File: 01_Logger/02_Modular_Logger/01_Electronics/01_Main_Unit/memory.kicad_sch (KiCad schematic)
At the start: 3 parts, among them J701 Micro_SD_Card_Det

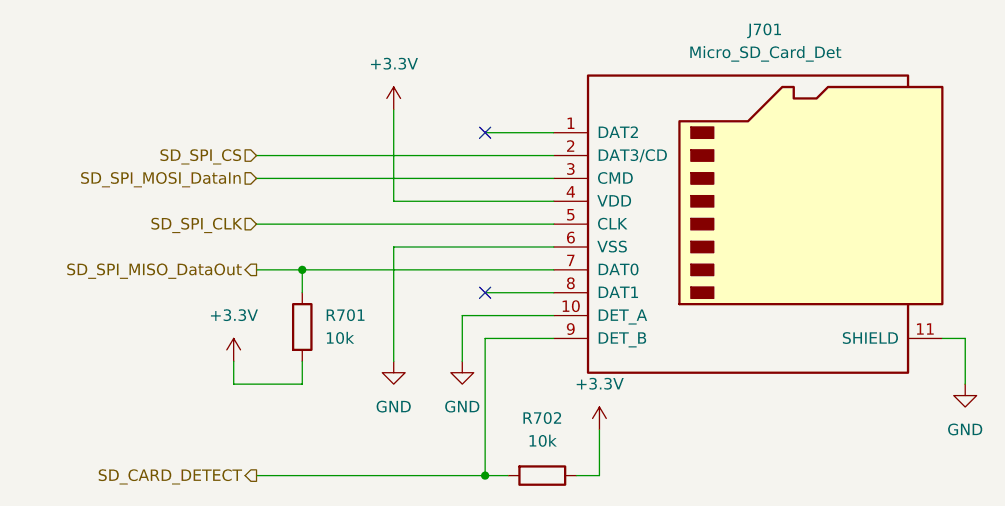
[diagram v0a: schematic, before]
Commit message: update Electronics for Modular_Logger
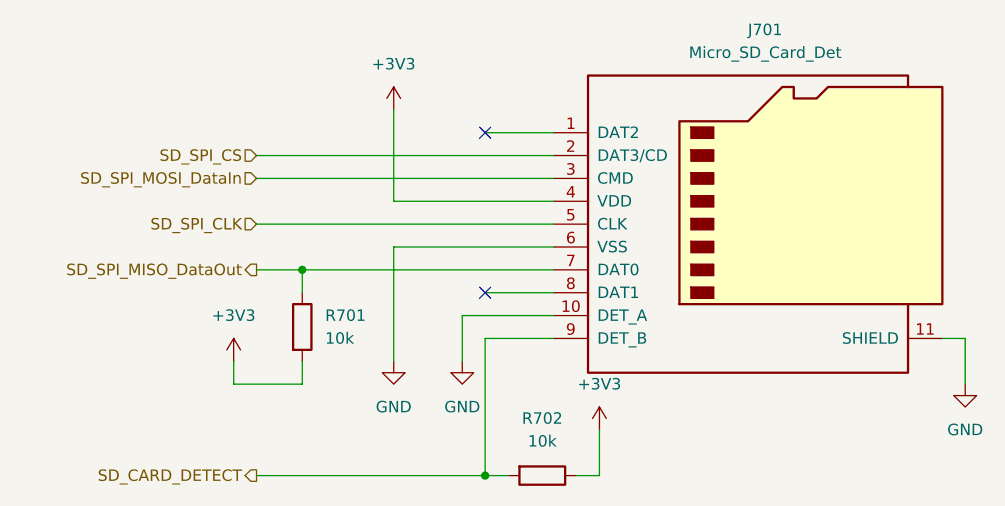
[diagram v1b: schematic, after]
